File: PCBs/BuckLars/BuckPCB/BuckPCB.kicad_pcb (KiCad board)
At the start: 2 copper layers, 33.5 x 47 mm, 15 parts, among them J1 IN, J2 OUT, J3 Measure, U1 LT1936

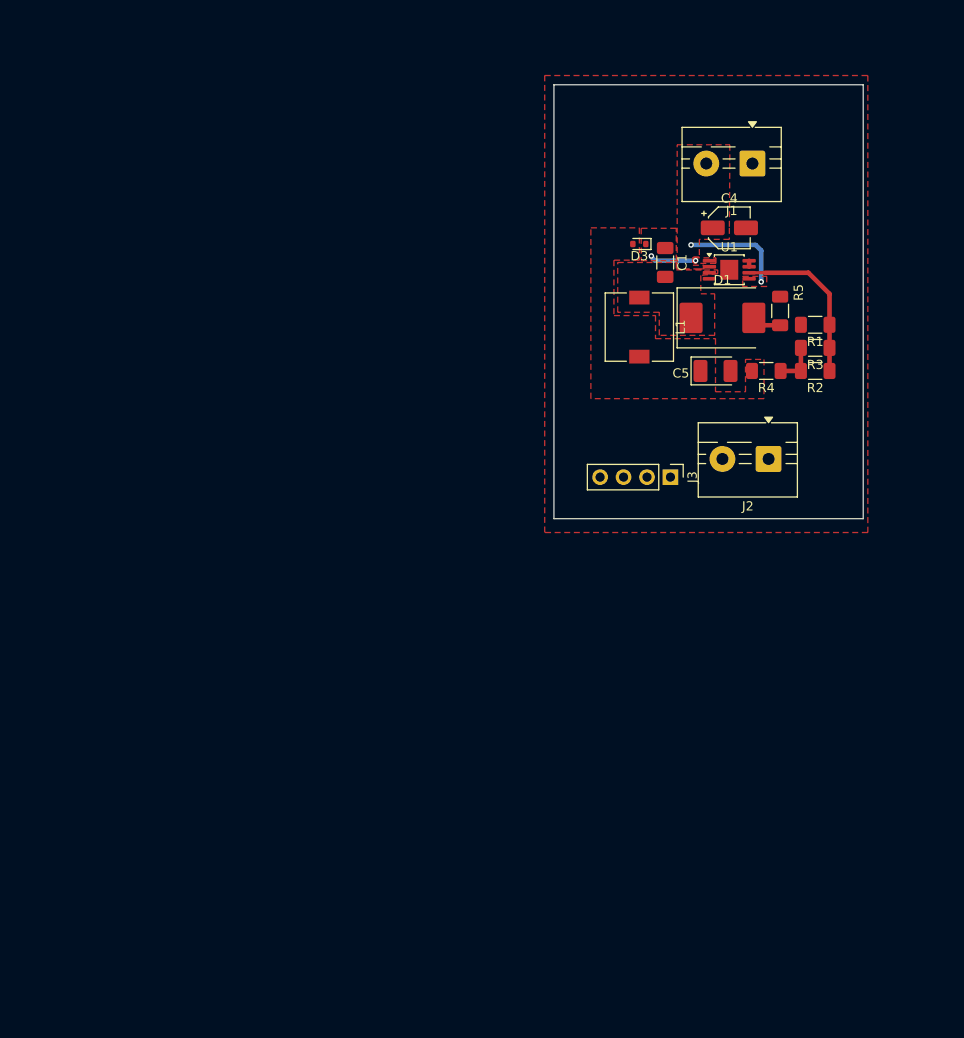
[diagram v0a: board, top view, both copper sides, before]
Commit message: cleanup chematic and assinged footprints
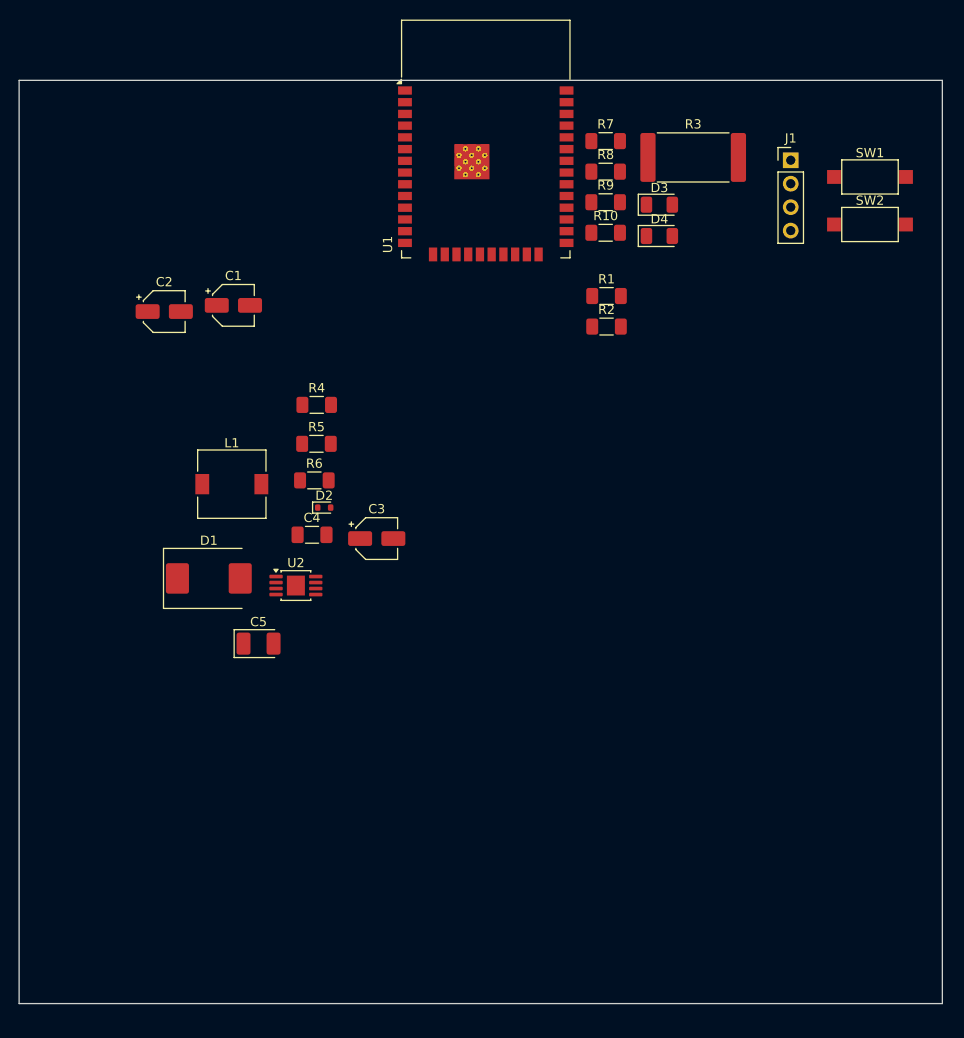
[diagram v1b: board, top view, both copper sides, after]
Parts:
- removed J2: OUT, TerminalBlock:TerminalBlock_MaiXu_MX126-5.0-02P_1x02_P5.00mm
- removed J3: Measure, Connector_PinHeader_2.54mm:PinHeader_1x04_P2.54mm_Vertical
- added C2: 10U, Capacitor_SMD:CP_Elec_4x5.3, F.Cu at (112.3, 86.8)
- added C3: 4.7uF 50V, Capacitor_SMD:CP_Elec_4x5.4, F.Cu at (135.3, 111.4)
- added D2: 1N4148WT, Diode_SMD:D_SOD-523, F.Cu at (129.6, 108.1)
- added D4: 3,3V, Diode_SMD:D_1206_3216Metric, F.Cu at (165.9, 78.6)
- added R10: 10k, Resistor_SMD:R_1206_3216Metric_Pad1.30x1.75mm_HandSolder, F.Cu at (160.1, 78.3)
- added R6: 560K, Resistor_SMD:R_1206_3216Metric_Pad1.30x1.75mm_HandSolder, F.Cu at (128.6, 105.1)
- added R7: 220k, Resistor_SMD:R_1206_3216Metric_Pad1.30x1.75mm_HandSolder, F.Cu at (160.1, 68.4)
- added R8: 10k, Resistor_SMD:R_1206_3216Metric_Pad1.30x1.75mm_HandSolder, F.Cu at (160.1, 71.7)
- added R9: 220k, Resistor_SMD:R_1206_3216Metric_Pad1.30x1.75mm_HandSolder, F.Cu at (160.1, 75.0)
- added SW1: RESET, Button_Switch_SMD:SW_SPST_CK_RS282G05A3, F.Cu at (188.7, 72.2)
- added SW2: Boot, Button_Switch_SMD:SW_SPST_CK_RS282G05A3, F.Cu at (188.7, 77.4)
- added U2: LT1936, Package_SO:MSOP-8-1EP_3x3mm_P0.65mm_EP1.95x2.15mm, F.Cu at (126.6, 116.5)
- C1: value 0.22uF -> 47U; footprint Capacitor_SMD:C_1206_3216Metric_Pad1.33x1.80mm_HandSolder -> Capacitor_SMD:CP_Elec_4x5.3
- C4: value 4.7uF -> 0.22uF; footprint Capacitor_SMD:CP_Elec_4x5.4 -> Capacitor_SMD:C_1206_3216Metric_Pad1.33x1.80mm_HandSolder
- D3: value 1N4148WT -> 3,3V; footprint Diode_SMD:D_SOD-523 -> Diode_SMD:D_1206_3216Metric
- J1: value IN -> Program_header; footprint TerminalBlock:TerminalBlock_MaiXu_MX126-5.0-02P_1x02_P5.00mm -> Connector_PinHeader_2.54mm:PinHeader_1x04_P2.54mm_Vertical
- R2: value 18K -> 10K
- R3: value 560K -> 0.05; footprint Resistor_SMD:R_1206_3216Metric_Pad1.30x1.75mm_HandSolder -> Resistor_SMD:R_4020_10251Metric_Pad1.65x5.30mm_HandSolder
- R4: value 22 -> 10K
- R5: value 0.1 -> 18K
- U1: value LT1936 -> ESP32-WROOM-32D; footprint Package_SO:MSOP-8-1EP_3x3mm_P0.65mm_EP1.95x2.15mm -> RF_Module:ESP32-WROOM-32D
- moved D1 62.4 mm to (117.1, 115.7)
- moved C5 57.6 mm to (122.5, 122.8)
- moved C4 56.1 mm to (128.3, 111.0)
- moved R5 52.2 mm to (128.8, 101.1), turned to 0 degrees
- moved R4 48.8 mm to (128.8, 96.9), turned to 0 degrees
- moved L1 47.3 mm to (119.6, 105.5), turned to 0 degrees
- moved C1 47.0 mm to (119.8, 86.1), turned to 0 degrees
- moved U1 28.6 mm to (147.1, 71.1)
- moved R3 24.5 mm to (169.6, 70.1), turned to 0 degrees
- moved R2 23.1 mm to (160.2, 88.4), turned to 0 degrees
- moved R1 22.8 mm to (160.2, 85.1), turned to 0 degrees
- moved D3 4.78 mm to (165.9, 75.2), turned to 0 degrees
- moved J1 4.16 mm to (180.1, 70.4), turned to 0 degrees
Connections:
- C1 pad 1: Net-(D3-K) -> Imeasure
- C1 pad 2: Usw -> GND
- C4 pad 1: VCC -> Net-(D2-K)
- C4 pad 2: GND -> Net-(D1-K)
- C5 pad 1: Uout -> +3.3V
- D1 pad 1: Usw -> Net-(D1-K)
- D1 pad 2: Id -> GND
- D3 pad 2: Uout -> GND
- J1 pad 1: GND -> +3.3V
- J1 pad 2: VCC -> Net-(J1-Pin_2)
- L1 pad 1: Usw -> Net-(D1-K)
- L1 pad 2: Uout -> +3.3V
- R1 pad 1: Net-(U1-FB) -> +3.3V
- R1 pad 2: GND -> Net-(U1-EN)
- R2 pad 1: Net-(U1-FB) -> +3.3V
- R2 pad 2: Net-(R2-Pad2) -> Net-(U1-IO0)
- R3 pad 1: Net-(U1-FB) -> +BATT
- R3 pad 2: Net-(R2-Pad2) -> Imeasure
- R4 pad 1: Net-(R2-Pad2) -> Net-(U2-FB)
- R4 pad 2: Uout -> GND
- R5 pad 1: GND -> Net-(U2-FB)
- R5 pad 2: Id -> +3.3V
- U1 pad 1: Net-(D3-K) -> GND
- U1 pad 2: VCC -> +3.3V
- U1 pad 3: Usw -> Net-(U1-EN)
- U1 pad 4: GND -> unconnected-(U1-SENSOR_VP-Pad4)
- U1 pad 5: VCC -> unconnected-(U1-SENSOR_VN-Pad5)
- U1 pad 6: Net-(U1-FB) -> unconnected-(U1-IO34-Pad6)
- U1 pad 7: Net-(U1-COMP) -> unconnected-(U1-IO35-Pad7)
- U1 pad 8: Net-(U1-COMP) -> unconnected-(U1-IO32-Pad8)
- U1 pad 9: GND -> unconnected-(U1-IO33-Pad9)
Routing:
- net Net-(U1-FB): track 18.0 -> 0.00 mm
- net VCC: track 11.2 -> 0.00 mm, vias 2 -> 0
- net Net-(D3-K): track 5.07 -> 0.00 mm, vias 2 -> 0
- net Net-(R2-Pad2): track 4.70 -> 0.00 mm
- net Id: track 3.18 -> 0.00 mm
- net Net-(U1-COMP): track 0.65 -> 0.00 mm
- removed copper zone on F.Cu, net GND
- removed copper zone on F.Cu, net Net-(D3-K)
- removed copper zone on F.Cu, net Uout
- removed copper zone on F.Cu, net Usw
- removed copper zone on F.Cu, net VCC
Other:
- board size 33.5 x 47 mm -> 100 x 100 mm

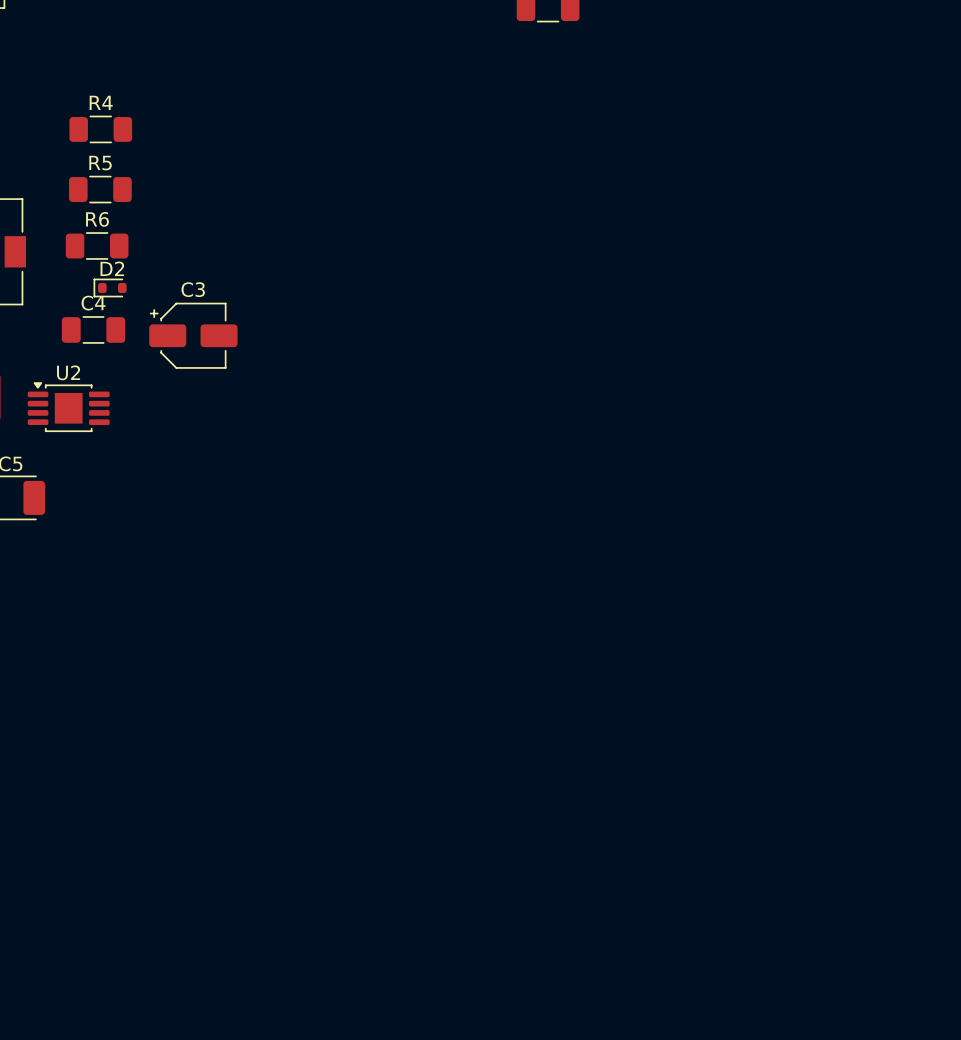
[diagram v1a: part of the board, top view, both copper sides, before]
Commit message: added buck converters schematic
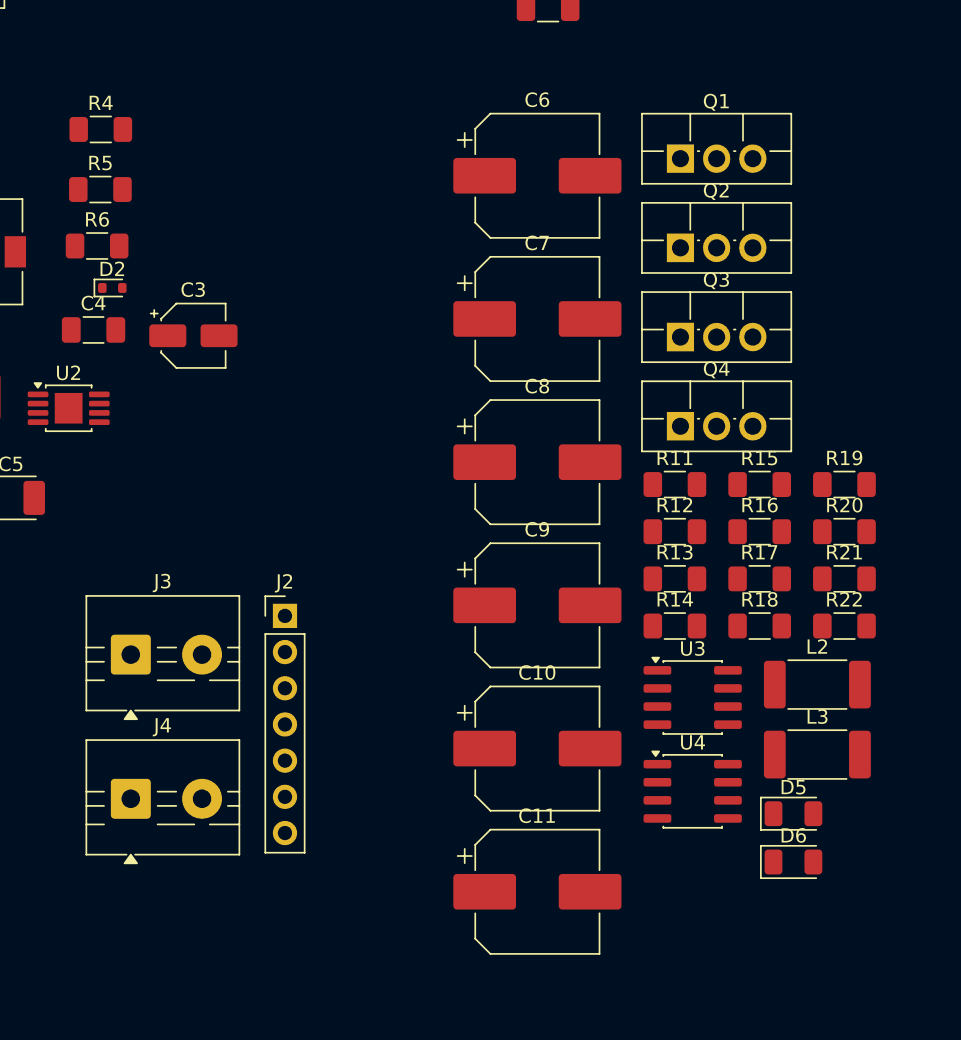
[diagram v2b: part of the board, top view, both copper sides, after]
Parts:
- added C10: 100u, Capacitor_SMD:CP_Elec_8x10.5, F.Cu at (159.4, 140.4)
- added C11: 100u, Capacitor_SMD:CP_Elec_8x10.5, F.Cu at (159.4, 150.4)
- added C6: C_Polarized, Capacitor_SMD:CP_Elec_8x10.5, F.Cu at (159.4, 100.2)
- added C7: 100u, Capacitor_SMD:CP_Elec_8x10.5, F.Cu at (159.4, 110.2)
- added C8: C_Polarized, Capacitor_SMD:CP_Elec_8x10.5, F.Cu at (159.4, 120.3)
- added C9: 100u, Capacitor_SMD:CP_Elec_8x10.5, F.Cu at (159.4, 130.3)
- added D5: 3,3V, Diode_SMD:D_1206_3216Metric, F.Cu at (177.4, 144.9)
- added D6: 3,3V, Diode_SMD:D_1206_3216Metric, F.Cu at (177.4, 148.3)
- added J2: Main board header, Connector_PinHeader_2.54mm:PinHeader_1x07_P2.54mm_Vertical, F.Cu at (141.7, 131.1)
- added J3: 12V, TerminalBlock:TerminalBlock_MaiXu_MX126-5.0-02P_1x02_P5.00mm, F.Cu at (130.9, 133.8)
- added J4: 5V, TerminalBlock:TerminalBlock_MaiXu_MX126-5.0-02P_1x02_P5.00mm, F.Cu at (130.9, 143.9)
- added L2: L, Inductor_SMD:L_2512_6332Metric_Pad1.52x3.35mm_HandSolder, F.Cu at (179.1, 135.9)
- added L3: L, Inductor_SMD:L_2512_6332Metric_Pad1.52x3.35mm_HandSolder, F.Cu at (179.1, 140.8)
- added Q1: IRLIZ44N, Package_TO_SOT_THT:TO-220F-3_Vertical, F.Cu at (169.5, 99.0)
- added Q2: IRLIZ44N, Package_TO_SOT_THT:TO-220F-3_Vertical, F.Cu at (169.5, 105.2)
- added Q3: IRLIZ44N, Package_TO_SOT_THT:TO-220F-3_Vertical, F.Cu at (169.5, 111.5)
- added Q4: IRLIZ44N, Package_TO_SOT_THT:TO-220F-3_Vertical, F.Cu at (169.5, 117.8)
- added R11: 10, Resistor_SMD:R_1206_3216Metric_Pad1.30x1.75mm_HandSolder, F.Cu at (169.1, 121.8)
- added R12: 10, Resistor_SMD:R_1206_3216Metric_Pad1.30x1.75mm_HandSolder, F.Cu at (169.1, 125.2)
- added R13: 10, Resistor_SMD:R_1206_3216Metric_Pad1.30x1.75mm_HandSolder, F.Cu at (169.1, 128.5)
- added R14: 10, Resistor_SMD:R_1206_3216Metric_Pad1.30x1.75mm_HandSolder, F.Cu at (169.1, 131.8)
- added R15: 0.1, Resistor_SMD:R_1206_3216Metric_Pad1.30x1.75mm_HandSolder, F.Cu at (175.0, 121.8)
- added R16: 0.1, Resistor_SMD:R_1206_3216Metric_Pad1.30x1.75mm_HandSolder, F.Cu at (175.0, 125.2)
- added R17: 39k, Resistor_SMD:R_1206_3216Metric_Pad1.30x1.75mm_HandSolder, F.Cu at (175.0, 128.5)
- added R18: 10k, Resistor_SMD:R_1206_3216Metric_Pad1.30x1.75mm_HandSolder, F.Cu at (175.0, 131.8)
- added R19: 10k, Resistor_SMD:R_1206_3216Metric_Pad1.30x1.75mm_HandSolder, F.Cu at (181.0, 121.8)
- added R20: 10k, Resistor_SMD:R_1206_3216Metric_Pad1.30x1.75mm_HandSolder, F.Cu at (181.0, 125.2)
- added R21: 100K, Resistor_SMD:R_1206_3216Metric_Pad1.30x1.75mm_HandSolder, F.Cu at (181.0, 128.5)
- added R22: 100k, Resistor_SMD:R_1206_3216Metric_Pad1.30x1.75mm_HandSolder, F.Cu at (181.0, 131.8)
- added U3: LF2304NTR, Package_SO:SOIC-8_3.9x4.9mm_P1.27mm, F.Cu at (170.3, 136.8)
- added U4: LF2304NTR, Package_SO:SOIC-8_3.9x4.9mm_P1.27mm, F.Cu at (170.3, 143.4)
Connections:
- D3 pad 1: Net-(D3-K) -> Vb
- D4 pad 1: Net-(D4-K) -> Vm
- R10 pad 1: Net-(D4-K) -> Vm
- R7 pad 2: Net-(D3-K) -> Vb
- R8 pad 1: Net-(D3-K) -> Vb
- R9 pad 2: Net-(D4-K) -> Vm
- U1 pad 10: unconnected-(U1-IO25-Pad10) -> Vm
- U1 pad 11: unconnected-(U1-IO26-Pad11) -> V5
- U1 pad 28: Net-(D4-K) -> unconnected-(U1-IO17-Pad28)
- U1 pad 30: Net-(D3-K) -> unconnected-(U1-IO18-Pad30)
- U1 pad 33: unconnected-(U1-IO21-Pad33) -> SDA
- U1 pad 36: unconnected-(U1-IO22-Pad36) -> SCL
- U1 pad 6: unconnected-(U1-IO34-Pad6) -> V12
- U1 pad 7: unconnected-(U1-IO35-Pad7) -> Vb
- U2 pad 9: (no net) -> GND

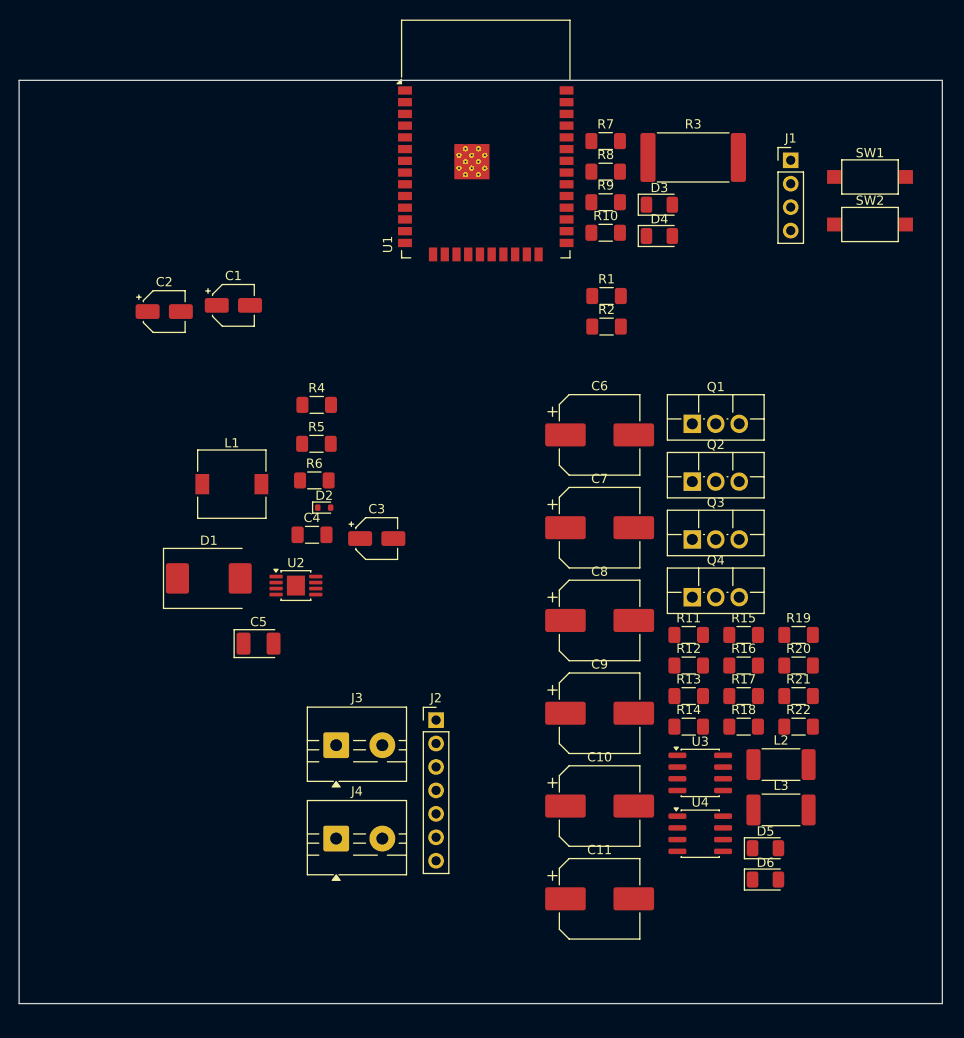
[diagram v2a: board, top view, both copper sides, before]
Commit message: wired buck converter pcb
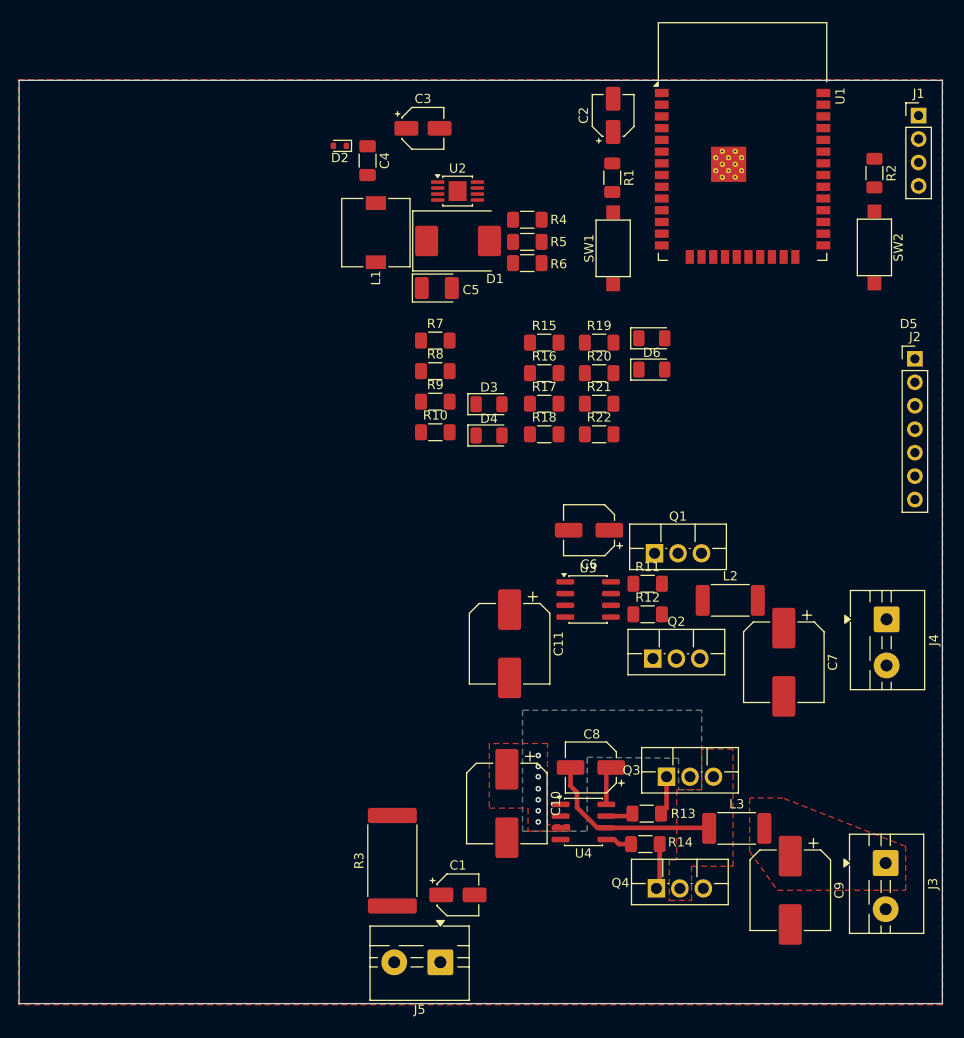
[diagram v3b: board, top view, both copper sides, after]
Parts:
- added J5: POWER_IN, TerminalBlock:TerminalBlock_MaiXu_MX126-5.0-02P_1x02_P5.00mm, F.Cu at (142.2, 157.3)
- C6, C8: footprint Capacitor_SMD:CP_Elec_8x10.5 -> Capacitor_SMD:CP_Elec_5x5.4
- SW2: value Boot -> BOOT
- moved R3 82.9 mm to (137.0, 146.3), turned to 90 degrees
- moved C1 68.3 mm to (144.1, 150.0)
- moved J2 65.0 mm to (193.6, 91.9)
- moved J4 64.2 mm to (190.5, 120.2), turned to -90 degrees
- moved J3 60.9 mm to (190.4, 146.6), turned to -90 degrees
- moved D6 56.6 mm to (165.1, 93.1)
- moved D5 56.6 mm to (165.1, 89.7)
- moved C2 53.1 mm to (160.9, 65.6), turned to 90 degrees
- moved U2 46.2 mm to (144.1, 73.8)
- moved D1 45.4 mm to (144.1, 79.2)
- moved C3 44.7 mm to (140.3, 67.0)
- moved C5 43.1 mm to (141.8, 84.3)
- moved C4 41.0 mm to (134.3, 70.5), turned to -90 degrees
- moved D2 39.2 mm to (131.3, 68.9), turned to 180 degrees
- moved R16 38.3 mm to (153.4, 93.5)
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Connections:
- C10 pad 1: +BATT -> Imeasure
- C11 pad 1: +BATT -> Imeasure
- Q1 pad 2: +BATT -> Imeasure
- Q3 pad 2: +BATT -> Imeasure
- R1 pad 2: Net-(U1-EN) -> Net-(SW1-B)
- R2 pad 2: Net-(U1-IO0) -> Net-(SW2-A)
- SW1 pad 2: GND -> Net-(SW1-B)
- SW2 pad 1: GND -> Net-(SW2-A)
- U1 pad 10: Vm -> LO1
- U1 pad 11: V5 -> HI2
- U1 pad 12: unconnected-(U1-IO27-Pad12) -> LO2
- U1 pad 25: Net-(U1-IO0) -> Net-(SW2-A)
- U1 pad 3: Net-(U1-EN) -> Net-(SW1-B)
- U1 pad 37: unconnected-(U1-IO23-Pad37) -> HI1
- U1 pad 8: unconnected-(U1-IO32-Pad8) -> Vm
- U1 pad 9: unconnected-(U1-IO33-Pad9) -> V5
- U3 pad 1: unconnected-(U3-LIN-Pad1) -> LO1
- U3 pad 2: unconnected-(U3-HIN-Pad2) -> HI1
- U3 pad 3: +BATT -> Imeasure
- U4 pad 1: unconnected-(U4-LIN-Pad1) -> LO2
- U4 pad 2: unconnected-(U4-HIN-Pad2) -> HI2
- U4 pad 3: +BATT -> Imeasure
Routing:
- net Net-(Q3-S): track 0.00 -> 19.9 mm
- net Net-(Q4-G): track 0.00 -> 4.94 mm
- net Net-(Q3-G): track 0.00 -> 4.25 mm
- net Net-(U4-VB): track 0.00 -> 4.21 mm
- net Net-(U4-HO): track 0.00 -> 2.93 mm
- net Net-(U4-LO): track 0.00 -> 2.88 mm
- net +BATT: vias 0 -> 7
- added copper zone on B.Cu, net +BATT
- added copper zone on F.Cu, net +BATT
- added copper zone on F.Cu, net GND
- added copper zone on F.Cu, net Net-(C9-Pad1)
- added copper zone on F.Cu, net Net-(Q3-S)
